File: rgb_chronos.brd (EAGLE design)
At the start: 29.4 x 12.2 mm, 24 parts

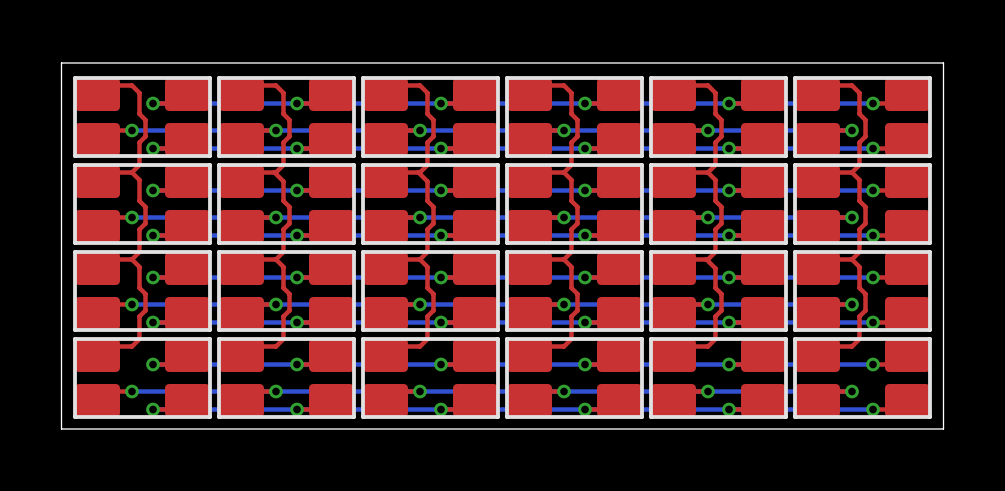
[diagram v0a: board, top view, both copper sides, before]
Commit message: Display nets renamed
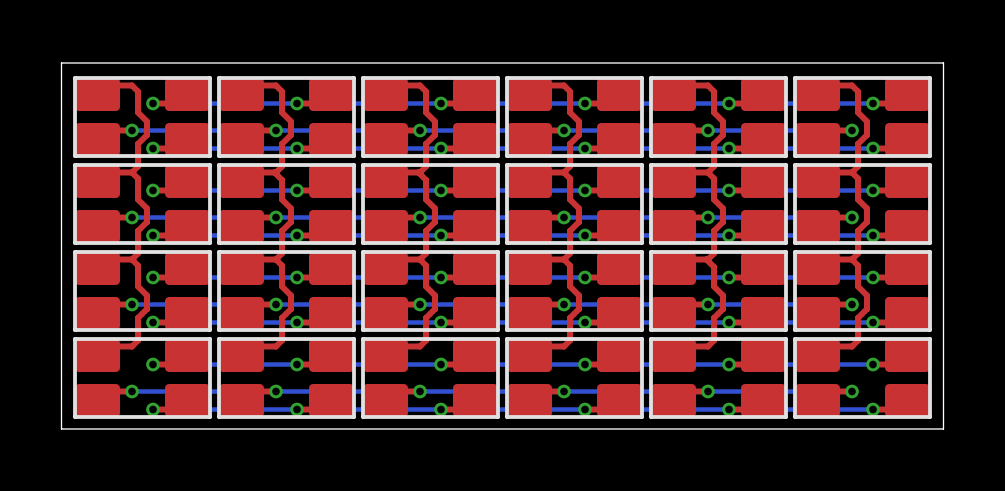
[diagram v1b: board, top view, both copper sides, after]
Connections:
- net N$1 renamed COL0
- net N$10 renamed ROW3_R
- net N$11 renamed ROW2_G
- net N$12 renamed ROW2_B
- net N$13 renamed ROW1_R
- net N$14 renamed ROW1_G
- net N$15 renamed ROW1_B
- net N$16 renamed ROW0_R
- net N$17 renamed ROW0_G
- net N$18 renamed ROW0_B
- net N$2 renamed COL5
- net N$3 renamed COL4
- net N$4 renamed COL3
- net N$5 renamed COL2
- net N$6 renamed COL1
- net N$7 renamed ROW2_R
- net N$8 renamed ROW3_B
- net N$9 renamed ROW3_G

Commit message: Added LED part number
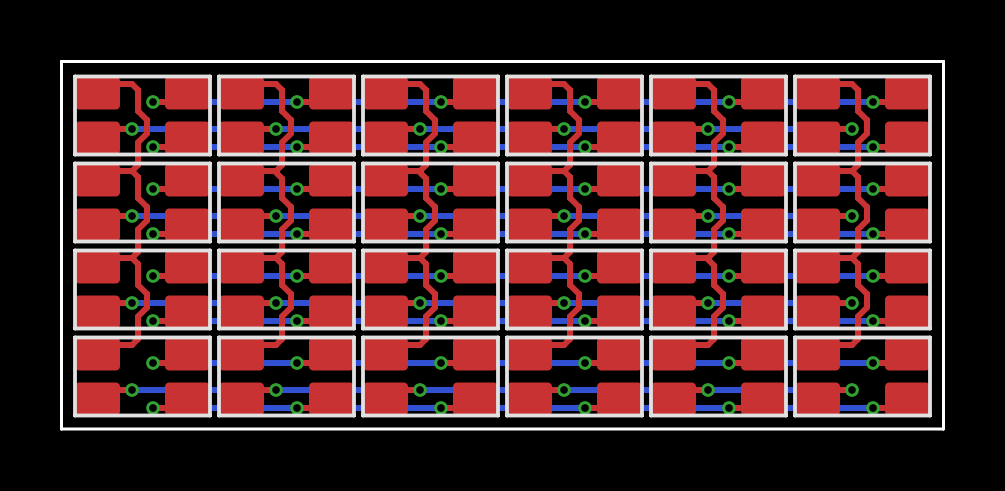
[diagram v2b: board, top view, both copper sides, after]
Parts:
- U$1, U$10, U$11, U$12, U$13, U$14, U$15, U$16, U$17, U$18, U$19, U$2, U$20, U$21, U$22, U$23, U$24, U$3, U$4, U$5, U$6, U$7, U$8, U$9: value LED3_ARGB -> ASMB-MTB0-0A3A2
- moved U$10 0.05 mm to (17.1, 4.65)
- moved U$14 0.05 mm to (12.3, 4.65)
- moved U$18 0.05 mm to (7.50, 4.65)
- moved U$2 0.05 mm to (26.7, 4.65)
- moved U$22 0.05 mm to (2.70, 4.65)
- moved U$6 0.05 mm to (21.9, 4.65)
- moved U$1 0.05 mm to (26.7, 1.75)
- moved U$13 0.05 mm to (12.3, 1.75)
- moved U$17 0.05 mm to (7.50, 1.75)
- moved U$21 0.05 mm to (2.70, 1.75)
- moved U$5 0.05 mm to (21.9, 1.75)
- moved U$9 0.05 mm to (17.1, 1.75)
